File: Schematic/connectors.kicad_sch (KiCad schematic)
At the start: 32 parts, among them J10 PIN2216, J11 PIN2216, J12 PIN2216, J2 PIN2216, J3 PIN2216, J4 PIN2216, J5 PIN2216, J6 PIN2216, J7 PIN2216, J8 PIN2216, J9 PIN2216, U14 HDGC1002WR-S-4P, U15 HDGC1002WR-S-4P, U16 HDGC1002WR-S-4P, U17 HDGC1002WR-S-4P, U19 HDGC1002WR-S-4P, U21 HDGC1002WR-S-8P, U22 HDGC1002WR-S-8P, U23 HDGC1002WR-S-6P, U24 HDGC1002WR-S-4P

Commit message: Refactor code structure for improved readability and maintainability
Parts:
- removed RN1, RN2: 100Ω, fch7_fp:RES-ARRAY-SMD_0603-8P-L3.2-W1.6-BL, symbol fch7_sym:4D03WGJ0101T5E
- removed U15, U16, U17, U19, U24: HDGC1002WR-S-4P, fch7_fp:SM03B-SRSS-TB(LF)(SN), symbol fclib:HDGC1002WR-S-4P
- removed U21, U22: HDGC1002WR-S-8P, fch7_fp:CONN-SMD_HDGC1002WR-S-8P, symbol fclib:HDGC1002WR-S-8P
- removed U23: HDGC1002WR-S-6P, fch7_fp:CONN-SMD_HDGC1002WR-S-6P, symbol fclib:HDGC1002WR-S-6P
- added RN1, RN2: 100Ω, fch7_fp:RES-ARRAY-SMD_0603-8P-L3.2-W1.6-BL, symbol fclib:4D03WGJ0101T5E
- added U10, U11, U7, U8, U9: HDGC1002WR-S-4P, fch7_fp:CONN-SMD_4P-P1.00_HDGC_HDGC1002WR-S-4P, symbol fclib:HDGC1002WR-S-4P
- added U15: HDGC1002WR-S-6P, fch7_fp:CONN-SMD_HDGC1002WR-S-6P, symbol fclib:HDGC1002WR-S-6P
- added U16, U17: HDGC1002WR-S-8P, fch7_fp:CONN-SMD_HDGC1002WR-S-8P, symbol fclib:HDGC1002WR-S-8P
- U14: footprint fch7_fp:SM03B-SRSS-TB(LF)(SN) -> fch7_fp:CONN-SMD_4P-P1.00_HDGC_HDGC1002WR-S-4P
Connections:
- net 4V5: now also U14.4, U10.2, U11.2, U7.2, U8.2, U9.2; no longer U14.2
- net 9V_BEC: now also U15.1
- net GND: now also U10.1, U10.5, U10.6, U11.1, U11.5, U11.6, U15.2, U15.5, U15.7, U15.8, U16.1, U16.10, U17.1, U17.9, U7.1, U7.5, U7.6, U8.1, U8.5, U8.6, U9.1, U9.5, U9.6
- net I2C1_CLK: now also U14.2
- net I2C1_SDA: now also U14.3
- net PWM_1: now also RN2.5
- net PWM_2: now also RN2.6
- net PWM_3: now also RN2.7
- net PWM_4: now also RN2.8
- net PWM_5: now also RN1.8
- net PWM_6: now also RN1.7
- net PWM_7: now also RN1.6
- net PWM_8: now also RN1.5
- net SENS_CUR1: now also U17.4
- net SENS_CUR2: now also U16.4
- net UART1_RX: now also U7.3; no longer U14.3
- net UART1_TX: now also U7.4; no longer U14.4
- net UART2_RX: now also U8.3
- net UART2_TX: now also U8.4
- net UART3_RX: now also U15.4
- net UART3_TX: now also U15.3
- net UART4_RX: now also U9.3
- net UART4_TX: now also U9.4
- net UART6_RX: now also U10.3, U15.6
- net UART6_TX: now also U10.4
- net UART7_RX: now also U17.3
- net UART8_RX: now also U11.3
- net UART8_TX: now also U11.4
- net VBAT: now also U16.2, U16.3, U16.9, U17.10, U17.2
- new net: RN2.1, U17.8
- new net: RN2.2, U17.7
- new net: RN2.3, U17.6
- new net: RN2.4, U17.5
- new net: RN1.1, U16.8
- new net: RN1.2, U16.7
- new net: RN1.3, U16.6
- new net: RN1.4, U16.5

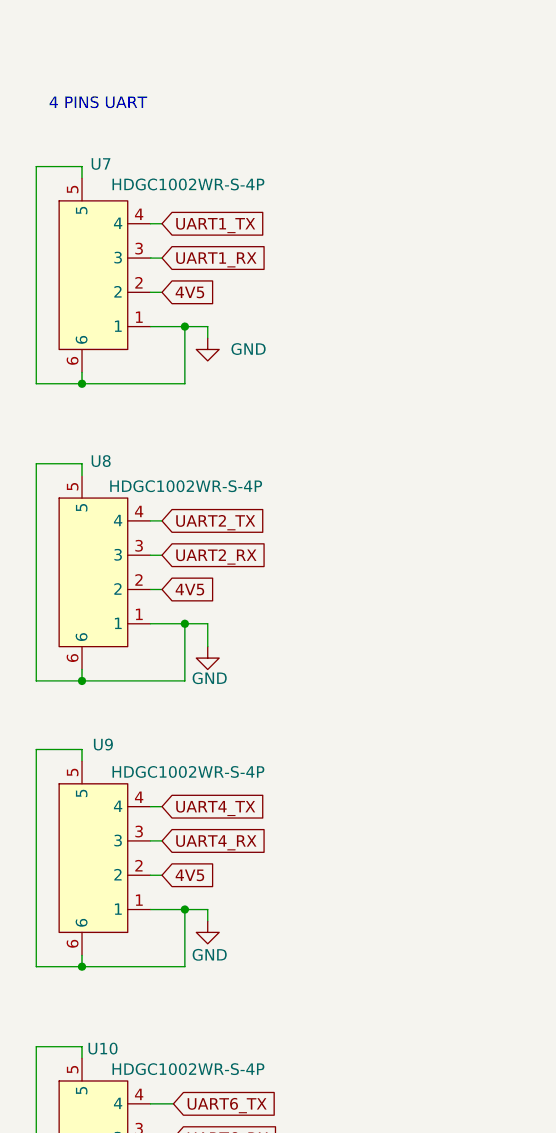
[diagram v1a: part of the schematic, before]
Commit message: Update schematic parameters and footprint information
- Modified differential pair dimensions to include a default gap, via gap, and width set to 0.0.
- Updated track widths to include a default value of 0.0.
- Added via dimensions with diameter and drill size set to 0.0.
- Adjusted track width for netclass settings, changing values for specific netclasses.
- Added new netclass entries for GND and POWER with corresponding patterns.
- Updated footprint info cache with a new identifier for the Audio Module.
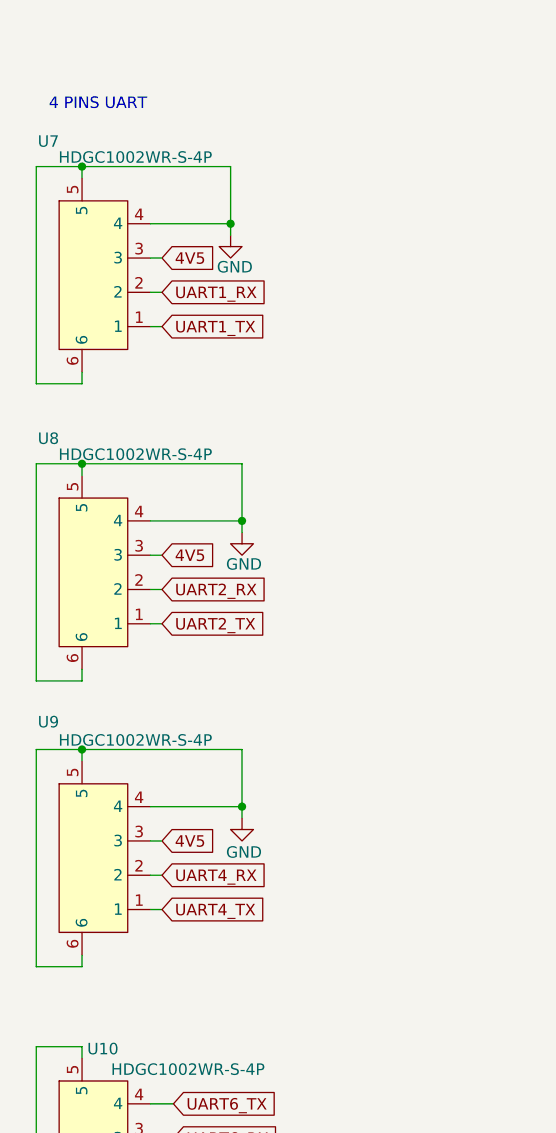
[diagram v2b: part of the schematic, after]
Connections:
- net 4V5: now also U7.3, U8.3, U9.3; no longer U7.2, U8.2, U9.2
- net GND: now also U7.4, U8.4, U9.4; no longer U7.1, U8.1, U9.1
- net UART1_RX: now also U7.2; no longer U7.3
- net UART1_TX: now also U7.1; no longer U7.4
- net UART2_RX: now also U8.2; no longer U8.3
- net UART2_TX: now also U8.1; no longer U8.4
- net UART4_RX: now also U9.2; no longer U9.3
- net UART4_TX: now also U9.1; no longer U9.4

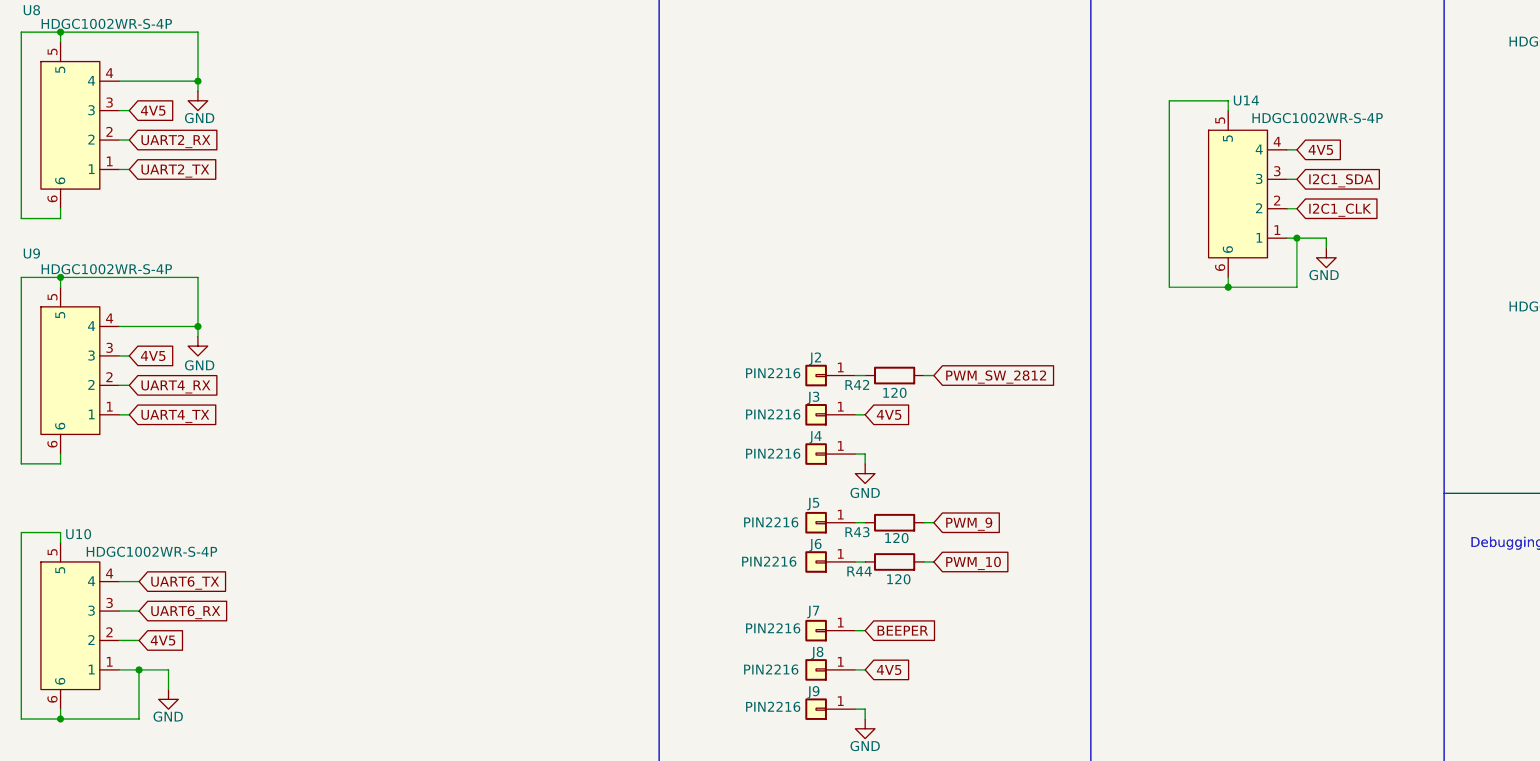
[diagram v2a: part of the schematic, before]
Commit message: Update schematic parameters and netclass definitions
- Reduced minimum via diameter from 0.8mm to 0.6mm for improved design flexibility.
- Removed redundant GND netclass configuration and adjusted POWER netclass priority.
- Added additional POWER netclasses for better organization and routing.
- Updated fp-info-cache with a new hash for the Audio_Module footprint.
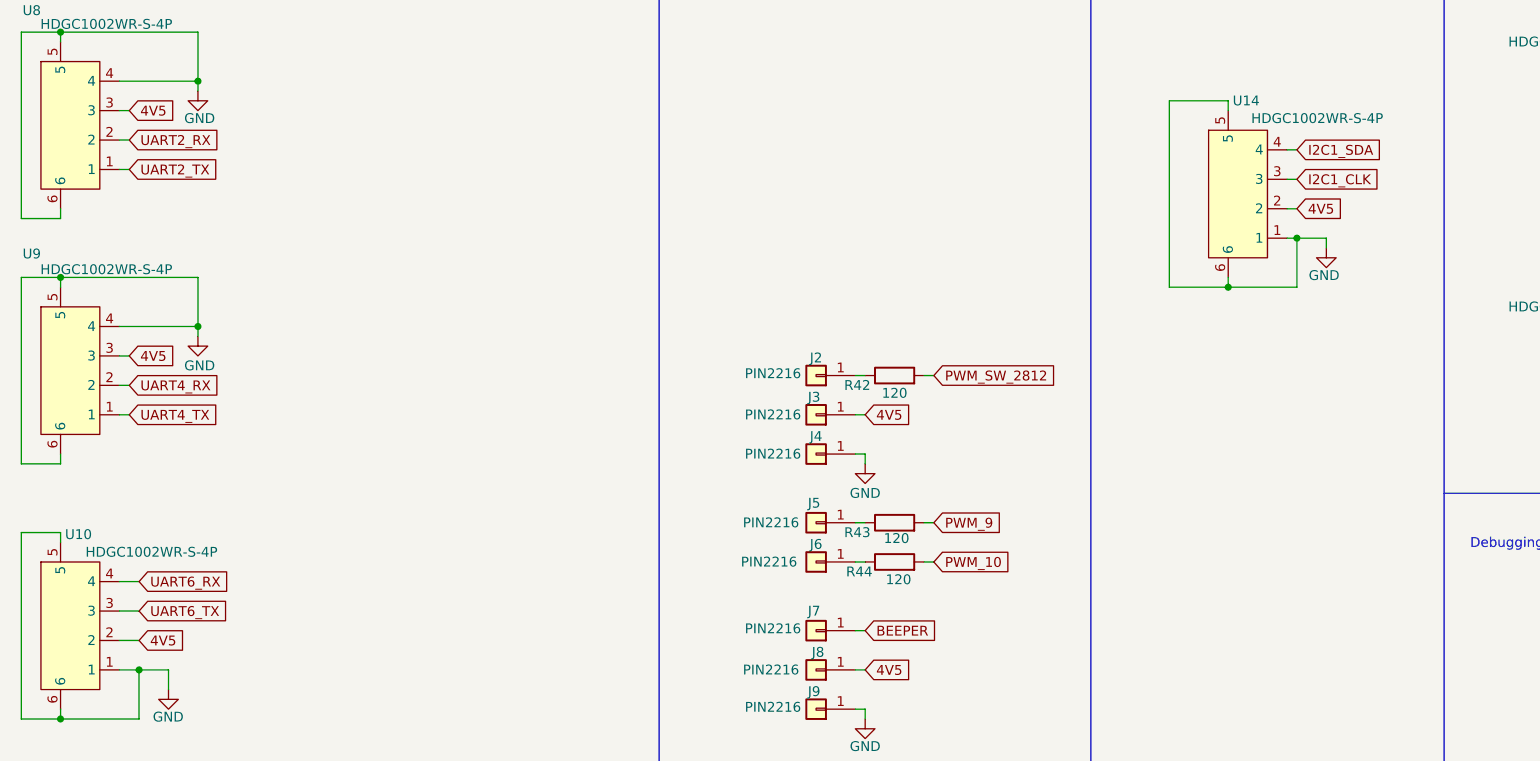
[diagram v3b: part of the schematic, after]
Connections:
- net 4V5: now also U14.2; no longer U14.4
- net I2C1_CLK: now also U14.3; no longer U14.2
- net I2C1_SDA: now also U14.4; no longer U14.3
- net UART6_RX: now also U10.4; no longer U10.3
- net UART6_TX: now also U10.3; no longer U10.4

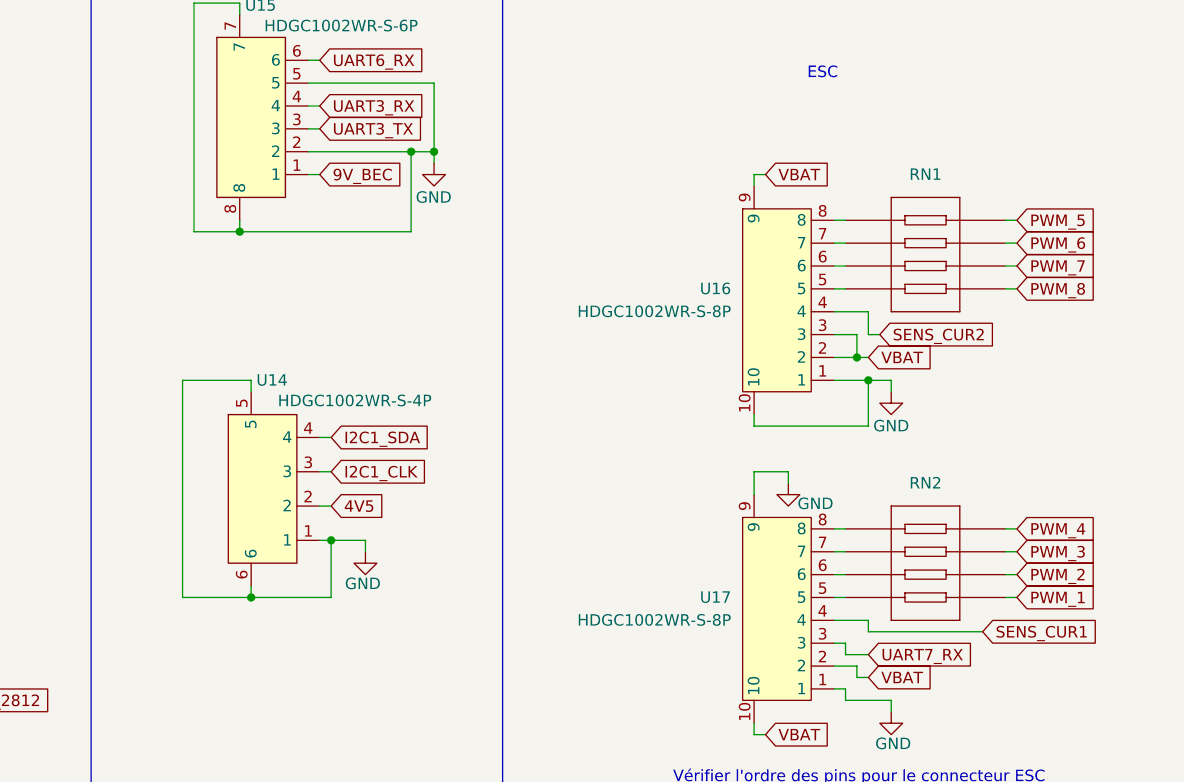
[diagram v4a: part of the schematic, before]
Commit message: Remove USB differential pair settings from schematic configuration and update footprint info cache for Audio_Module.
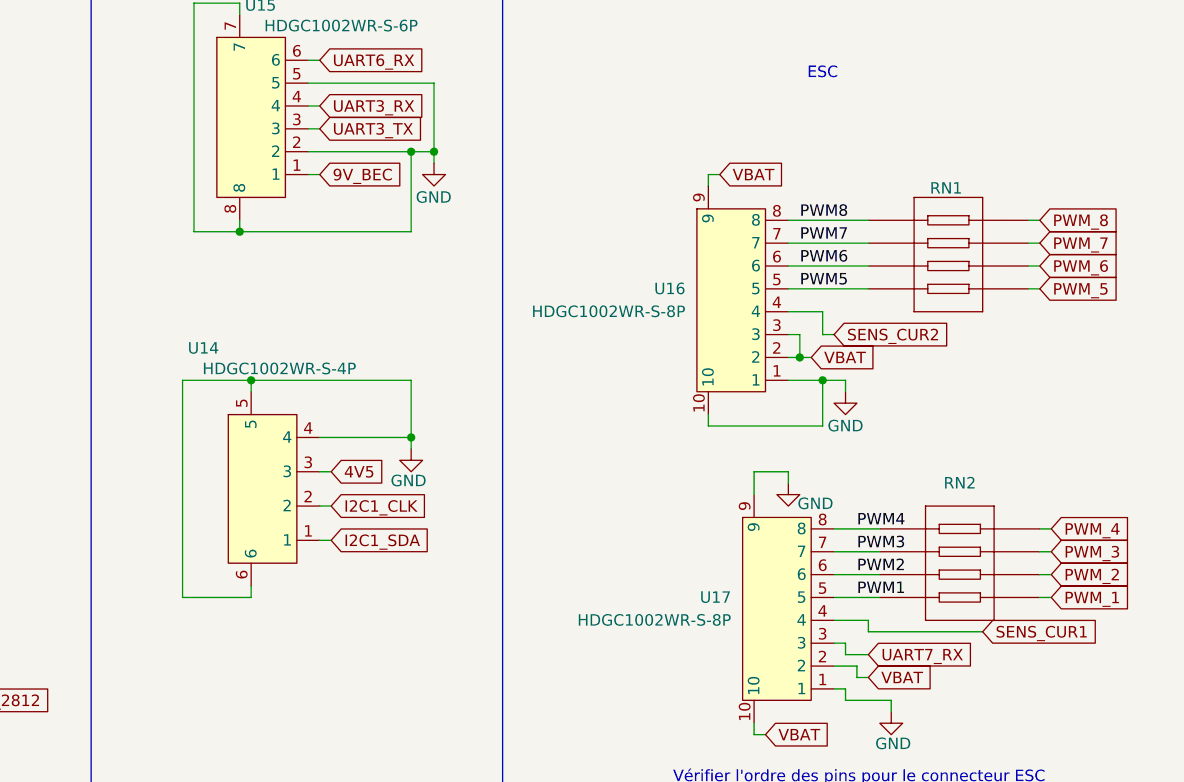
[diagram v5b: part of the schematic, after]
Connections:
- net 4V5: now also U14.3; no longer U14.2
- net GND: now also U14.4; no longer U14.1
- net I2C1_CLK: now also U14.2; no longer U14.3
- net I2C1_SDA: now also U14.1; no longer U14.4
- net PWM_5: now also RN1.5; no longer RN1.8
- net PWM_6: now also RN1.6; no longer RN1.7
- net PWM_7: now also RN1.7; no longer RN1.6
- net PWM_8: now also RN1.8; no longer RN1.5
- net PWM4: now reaches RN2.1, U17.8
- net PWM3: now reaches RN2.2, U17.7
- net PWM2: now reaches RN2.3, U17.6
- net PWM1: now reaches RN2.4, U17.5
- net PWM8: now reaches RN1.1, U16.8
- net PWM7: now reaches RN1.2, U16.7
- net PWM6: now reaches RN1.3, U16.6
- net PWM5: now reaches RN1.4, U16.5
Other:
- moved on the sheet: RN1, RN2, U16
